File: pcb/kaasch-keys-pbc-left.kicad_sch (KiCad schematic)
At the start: 73 parts, among them J1 Conn_01x12_Pin, J2 Conn_01x12_Pin, SW1 SW_Push, SW10 SW_Push, SW11 SW_Push, SW12 SW_Push, SW13 SW_Push, SW14 SW_Push, SW15 SW_Push, SW16 SW_Push, SW17 SW_Push, SW18 SW_Push, SW19 SW_Push, SW2 SW_Push, SW20 SW_Push, SW21 SW_Push, SW22 SW_Push, SW23 SW_Push, SW24 SW_Push, SW25 SW_Push, SW26 SW_Push, SW27 SW_Push, SW28 SW_Push, SW29 SW_Push, SW3 SW_Push, SW30 SW_Push, SW31 SW_Push, SW32 SW_Push, SW33 SW_Push, SW34 SW_Push, SW35 SW_Push, SW36 SW_Push_Reset, SW4 SW_Push, SW5 SW_Push, SW6 SW_Push, SW7 SW_Push, SW8 SW_Push, SW9 SW_Push

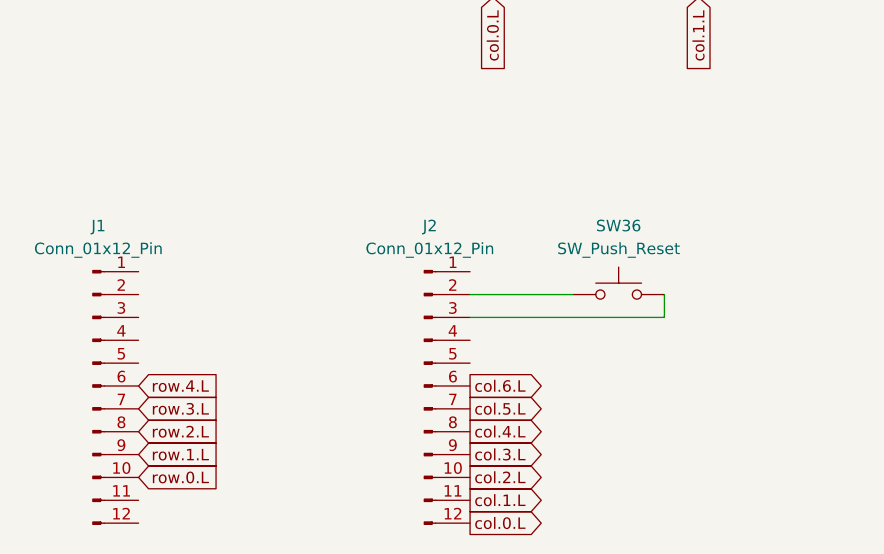
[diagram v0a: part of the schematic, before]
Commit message: left pcb complete and ready for testing
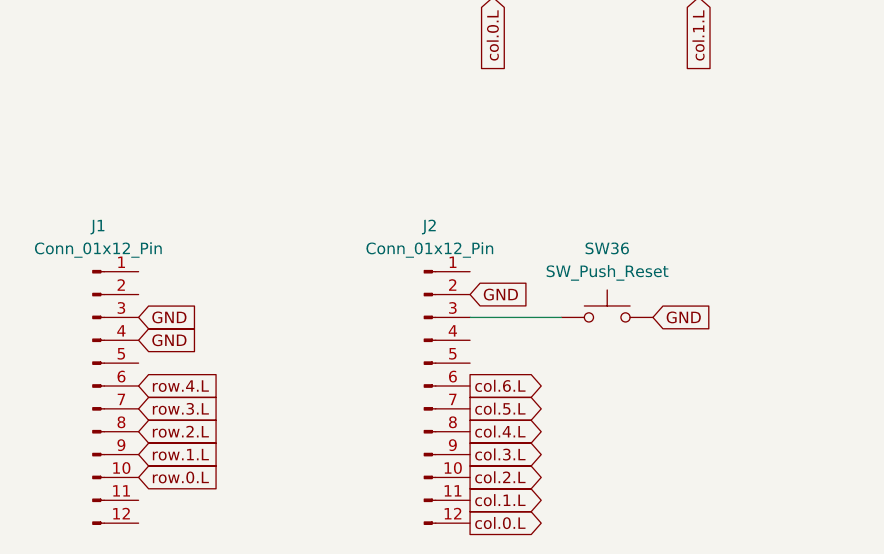
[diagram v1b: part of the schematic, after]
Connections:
- net at SW36.1: now also J2.3 (Pin_3); no longer J2.2 (Pin_2)
- net GND: now reaches SW36.2
- net GND: now also J1.3 (Pin_3), J1.4 (Pin_4), J2.2 (Pin_2); no longer J2.3 (Pin_3)
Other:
- moved on the sheet: SW36
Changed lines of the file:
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@@
-	(wire
-		(pts
-			(xy 106.68 154.94) (xy 95.25 154.94)
-		)
-		(stroke
-			(width 0)
-			(type default)
-		)
-	)
 	(wire
 		(pts
@@
 	(wire
 		(pts
+			(xy 95.25 157.48) (xy 105.41 157.48)
+		)
+		(stroke
+			(width 0)
+			(type default)
+		)
+	)
+	(wire
+		(pts
 			(xy 120.65 52.07) (xy 120.65 69.85)
 		)
@@
 	(wire
 		(pts
-			(xy 116.84 154.94) (xy 116.84 157.48)
-		)
-		(stroke
-			(width 0)
-			(type default)
-		)
-	)
-	(wire
-		(pts
 			(xy 199.39 113.03) (xy 199.39 125.73)
 		)
@@
 		(pts
 			(xy 130.81 59.69) (xy 153.67 59.69)
-		)
-		(stroke
-			(width 0)
-			(type default)
-		)
-	)
-	(wire
-		(pts
-			(xy 95.25 157.48) (xy 116.84 157.48)
 		)
 		(stroke
@@
 		)
 	)
+	(global_label "GND"
+		(shape input)
+		(at 58.42 157.48 0)
+		(fields_autoplaced yes)
+		(effects
+			(font
+				(size 1.27 1.27)
+			)
+			(justify left)
+		)
+		(property "Intersheetrefs" "${INTERSHEET_REFS}"
+			(at 65.2757 157.48 0)
+			(effects
+				(font
+					(size 1.27 1.27)
+				)
+				(justify left)
+				(hide yes)
+			)
+		)
+	)
 	(global_label "col.2.L"
 		(shape input)
@@
 		)
 	)
+	(global_label "GND"
+		(shape input)
+		(at 95.25 154.94 0)
+		(fields_autoplaced yes)
+		(effects
+			(font
+				(size 1.27 1.27)
+			)
+			(justify left)
+		)
+		(property "Intersheetrefs" "${INTERSHEET_REFS}"
+			(at 102.1057 154.94 0)
+			(effects
+				(font
+					(size 1.27 1.27)
+				)
+				(justify left)
+				(hide yes)
+			)
+		)
+	)
 	(global_label "col.0.L"
 		(shape input)
@@
 		)
 	)
+	(global_label "GND"
+		(shape input)
+		(at 58.42 160.02 0)
+		(fields_autoplaced yes)
+		(effects
+			(font
+				(size 1.27 1.27)
+			)
+			(justify left)
+		)
+		(property "Intersheetrefs" "${INTERSHEET_REFS}"
+			(at 65.2757 160.02 0)
+			(effects
+				(font
+					(size 1.27 1.27)
+				)
+				(justify left)
+				(hide yes)
+			)
+		)
+	)
 	(global_label "row.0.L"
 		(shape input)
@@
 		(property "Intersheetrefs" "${INTERSHEET_REFS}"
 			(at 68.1181 170.18 0)
+			(effects
+				(font
+					(size 1.27 1.27)
+				)
+				(justify left)
+				(hide yes)
+			)
+		)
+	)
+	(global_label "GND"
+		(shape input)
+		(at 115.57 157.48 0)
+		(fields_autoplaced yes)
+		(effects
+			(font
+				(size 1.27 1.27)
+			)
+			(justify left)
+		)
+		(property "Intersheetrefs" "${INTERSHEET_REFS}"
+			(at 122.4257 157.48 0)
 			(effects
 				(font
@@
 	(symbol
 		(lib_id "Switch:SW_Push")
-		(at 111.76 154.94 0)
+		(at 110.49 157.48 0)
 		(unit 1)
 		(exclude_from_sim no)
@@
 		(dnp no)
 		(property "Reference" "SW36"
-			(at 111.76 147.32 0)
+			(at 110.49 149.86 0)
 			(effects
 				(font
@@
 		)
 		(property "Value" "SW_Push_Reset"
-			(at 111.76 149.86 0)
+			(at 110.49 152.4 0)
 			(effects
 				(font
@@
 		)
 		(property "Footprint" "Button_Switch_SMD:SW_SPST_B3U-1000P"
-			(at 111.76 149.86 0)
+			(at 110.49 152.4 0)
 			(effects
 				(font
@@
 		)
 		(property "Datasheet" "~"
-			(at 111.76 149.86 0)
+			(at 110.49 152.4 0)
 			(effects
 				(font
@@
 		)
 		(property "Description" "Push button switch, generic, two pins"
-			(at 111.76 154.94 0)
-			(effects
-				(font
+			(at 110.49 157.48 0)
+			(effects
+				(font

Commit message: alternative thumb cluster position
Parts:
- SW30, SW34: footprint Button_Switch_Keyboard:SW_Cherry_MX_1.00u_PCB -> Button_Switch_Keyboard:SW_Cherry_MX_1.50u_PCB
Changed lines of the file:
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@@
 			)
 		)
-		(property "Footprint" "Button_Switch_Keyboard:SW_Cherry_MX_1.00u_PCB"
+		(property "Footprint" "Button_Switch_Keyboard:SW_Cherry_MX_1.50u_PCB"
 			(at 217.17 113.03 0)
 			(effects
@@
 			)
 		)
-		(property "Footprint" "Button_Switch_Keyboard:SW_Cherry_MX_1.00u_PCB"
+		(property "Footprint" "Button_Switch_Keyboard:SW_Cherry_MX_1.50u_PCB"
 			(at 240.03 113.03 0)
 			(effects

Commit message: continue on design
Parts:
- added J3: Conn_JST, Connector_JST:JST_EH_B2B-EH-A_1x02_P2.50mm_Vertical, symbol Connector:Conn_01x02_Pin
- added SW37: SW_Slide_Bat, Button_Switch_SMD:SW_SPDT_PCM12, symbol Switch:SW_SPDT
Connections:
- net GND: now also J3.2 (Pin_2)
- net RAW: now reaches J2.1 (Pin_1)
- net RAW: now also SW37.2 (B)
- new net BAT+: J3.1 (Pin_1), SW37.1 (A)
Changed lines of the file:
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@@
 		)
 	)
+	(global_label "BAT+"
+		(shape input)
+		(at 148.59 172.72 0)
+		(fields_autoplaced yes)
+		(effects
+			(font
+				(size 1.27 1.27)
+			)
+			(justify left)
+		)
+		(property "Intersheetrefs" "${INTERSHEET_REFS}"
+			(at 156.4738 172.72 0)
+			(effects
+				(font
+					(size 1.27 1.27)
+				)
+				(justify left)
+				(hide yes)
+			)
+		)
+	)
 	(global_label "row.0.L"
 		(shape input)
@@
 		)
 	)
+	(global_label "RAW"
+		(shape input)
+		(at 138.43 175.26 180)
+		(fields_autoplaced yes)
+		(effects
+			(font
+				(size 1.27 1.27)
+			)
+			(justify right)
+		)
+		(property "Intersheetrefs" "${INTERSHEET_REFS}"
+			(at 131.6348 175.26 0)
+			(effects
+				(font
+					(size 1.27 1.27)
+				)
+				(justify right)
+				(hide yes)
+			)
+		)
+	)
 	(global_label "GND"
 		(shape input)
@@
 		)
 	)
+	(global_label "RAW"
+		(shape input)
+		(at 95.25 152.4 0)
+		(fields_autoplaced yes)
+		(effects
+			(font
+				(size 1.27 1.27)
+			)
+			(justify left)
+		)
+		(property "Intersheetrefs" "${INTERSHEET_REFS}"
+			(at 102.0452 152.4 0)
+			(effects
+				(font
+					(size 1.27 1.27)
+				)
+				(justify left)
+				(hide yes)
+			)
+		)
+	)
 	(global_label "col.1.L"
 		(shape output)
@@
 		)
 	)
+	(global_label "GND"
+		(shape input)
+		(at 146.05 158.75 0)
+		(fields_autoplaced yes)
+		(effects
+			(font
+				(size 1.27 1.27)
+			)
+			(justify left)
+		)
+		(property "Intersheetrefs" "${INTERSHEET_REFS}"
+			(at 152.9057 158.75 0)
+			(effects
+				(font
+					(size 1.27 1.27)
+				)
+				(justify left)
+				(hide yes)
+			)
+		)
+	)
 	(global_label "row.4.L"
 		(shape output)
@@
 		)
 	)
+	(global_label "BAT+"
+		(shape input)
+		(at 146.05 156.21 0)
+		(fields_autoplaced yes)
+		(effects
+			(font
+				(size 1.27 1.27)
+			)
+			(justify left)
+		)
+		(property "Intersheetrefs" "${INTERSHEET_REFS}"
+			(at 153.9338 156.21 0)
+			(effects
+				(font
+					(size 1.27 1.27)
+				)
+				(justify left)
+				(hide yes)
+			)
+		)
+	)
 	(global_label "col.6.L"
 		(shape input)
@@
 	)
 	(symbol
+		(lib_id "Switch:SW_SPDT")
+		(at 143.51 175.26 0)
+		(unit 1)
+		(exclude_from_sim no)
+		(in_bom yes)
+		(on_board yes)
+		(dnp no)
+		(fields_autoplaced yes)
+		(property "Reference" "SW37"
+			(at 143.51 166.37 0)
+			(effects
+				(font
+					(size 1.27 1.27)
+				)
+			)
+		)
+		(property "Value" "SW_Slide_Bat"
+			(at 143.51 168.91 0)
+			(effects
+				(font
+					(size 1.27 1.27)
+				)
+			)
+		)
+		(property "Footprint" "Button_Switch_SMD:SW_SPDT_PCM12"
+			(at 143.51 175.26 0)
+			(effects
+				(font
+					(size 1.27 1.27)
+				)
+				(hide yes)
+			)
+		)
+		(property "Datasheet" "~"
+			(at 143.51 182.88 0)
+			(effects
+				(font
+					(size 1.27 1.27)
+				)
+				(hide yes)
+			)
+		)
+		(property "Description" "Switch, single pole double throw"
+			(at 143.51 175.26 0)
+			(effects
+				(font
+					(size 1.27 1.27)
+				)
+				(hide yes)
+			)
+		)
+		(pin "1"
+		)
+		(pin "3"
+		)
+		(pin "2"
+		)
+		(instances
+			(project ""
+				(path "/71cf87fc-58ce-4acc-b054-5cde32e406ee"
+					(reference "SW37")
+					(unit 1)
+				)
+			)
+		)
+	)
+	(symbol
 		(lib_id "Diode:1N4148")
 		(at 176.53 109.22 90)
@@
 					(unit 1)
 				)
+			)
+		)
+	)
+	(symbol
+		(lib_id "Connector:Conn_01x02_Pin")
+		(at 140.97 156.21 0)
+		(unit 1)
+		(exclude_from_sim no)
+		(in_bom yes)
+		(on_board yes)
+		(dnp no)
+		(fields_autoplaced yes)
+		(property "Reference" "J3"
+			(at 141.605 151.13 0)
+			(effects
+				(font
+					(size 1.27 1.27)
+				)
+			)
+		)
+		(property "Value" "Conn_JST"
+			(at 141.605 153.67 0)
+			(effects
+				(font
+					(size 1.27 1.27)
+				)
+			)
+		)
+		(property "Footprint" "Connector_JST:JST_EH_B2B-EH-A_1x02_P2.50mm_Vertical"
+			(at 140.97 156.21 0)
+			(effects
+				(font
+					(size 1.27 1.27)
+				)
+				(hide yes)
+			)
+		)
+		(property "Datasheet" "~"
+			(at 140.97 156.21 0)
+			(effects
+				(font
+					(size 1.27 1.27)
+				)
+				(hide yes)
+			)
+		)
+		(property "Description" "Generic connector, single row, 01x02, script generated"
+			(at 140.97 156.21 0)
+			(effects
+				(font
+					(size 1.27 1.27)
+				)
+				(hide yes)
+			)
+		)
+		(pin "1"
+		)
+		(pin "2"
+		)
+		(instances
+			(project ""
+				(path "/71cf87fc-58ce-4acc-b054-5cde32e406ee"
+					(reference "J3")
+					(unit 1)
+				)
